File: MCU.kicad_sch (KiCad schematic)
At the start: 44 parts, among them J12 PinHeader_01x03_Pin, SW11 KMR2, SW12 KMR2, U11 W25Q128JVS, U12 RP2350_60QFN, Y11 ABM8_262_T3

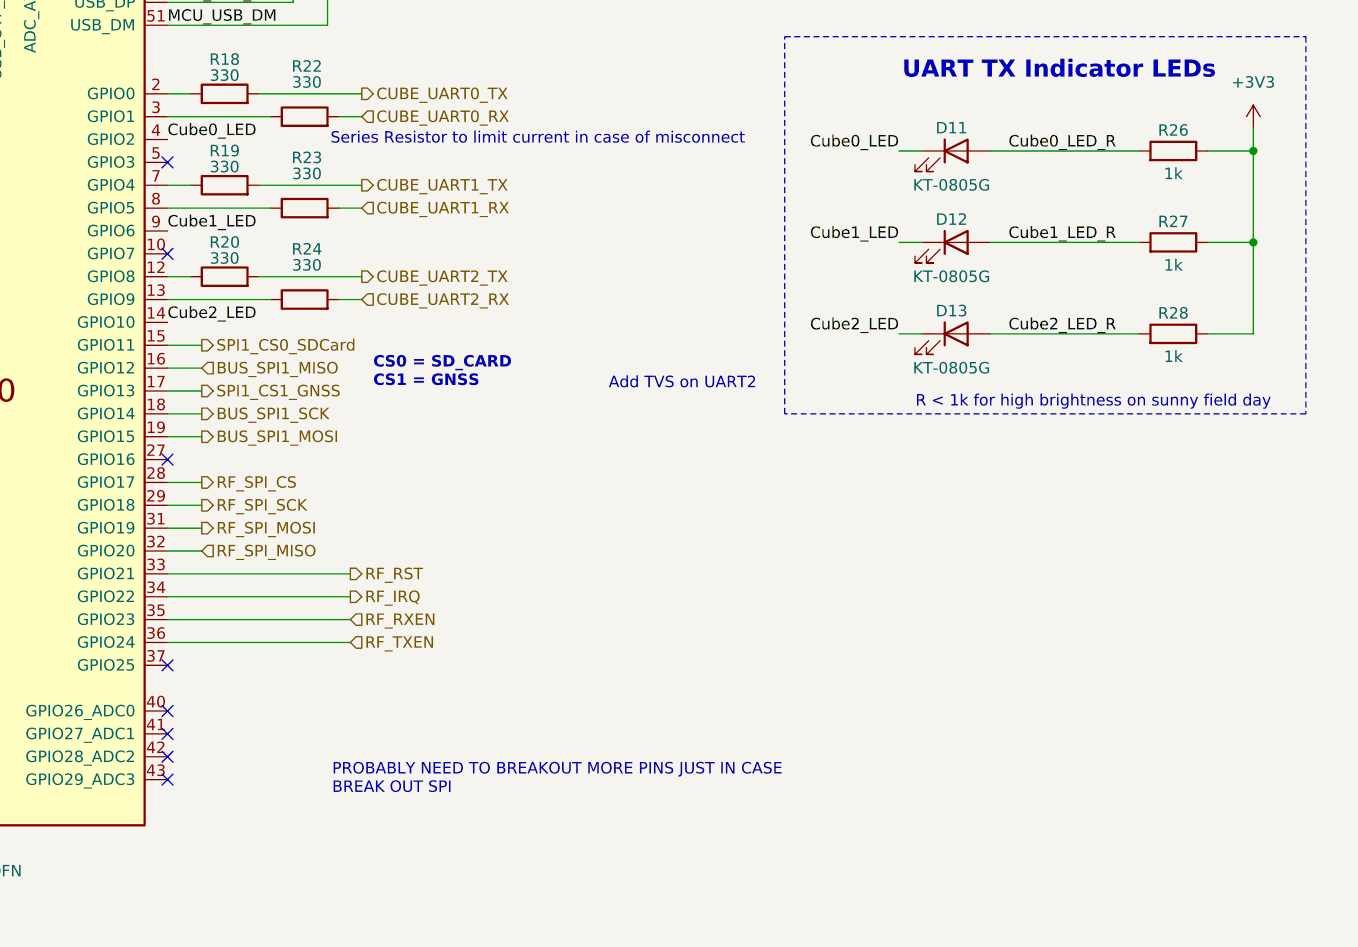
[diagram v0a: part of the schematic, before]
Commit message: discrete protection, charger, ideal diodes, and 5v smps
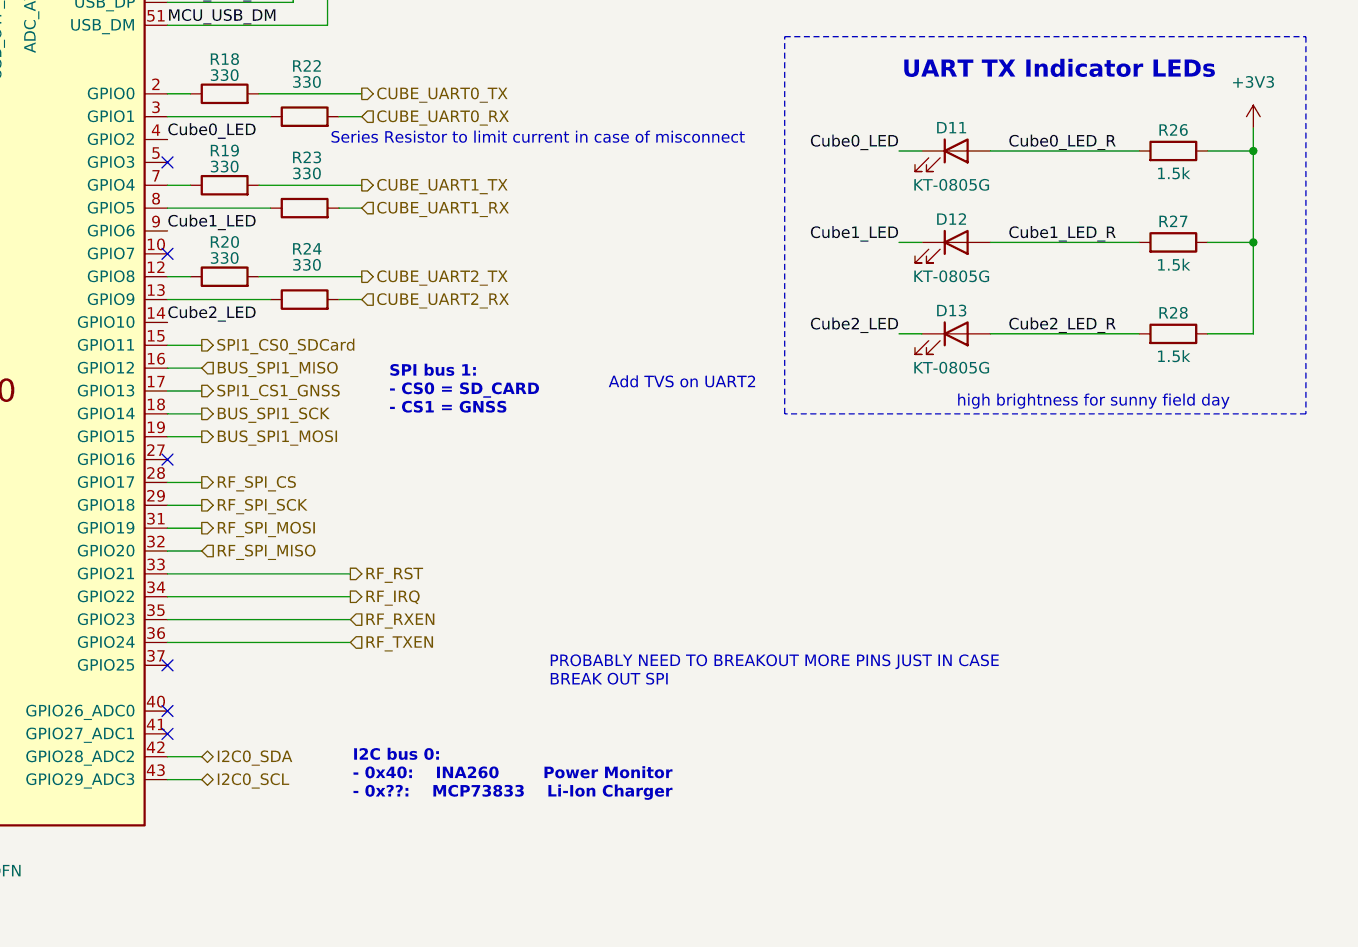
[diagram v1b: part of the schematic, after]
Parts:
- R26, R27, R28: value 1k -> 1.5k
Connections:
- net I2C0_SDA: now reaches U12.42 (GPIO28_ADC2)
- net I2C0_SCL: now reaches U12.43 (GPIO29_ADC3)
- no-connect marks 9 -> 7
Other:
- note added: "I2C bus 0: - 0x40: INA260 Power Monitor - 0x??: MCP73833 Li-Ion Charger"
- note added: "SPI bus 1: - CS0 = SD_CARD - CS1 = GNSS"
- note added: "high brightness for sunny field day"
- note removed: "CS0 = SD_CARD CS1 = GNSS"
- note removed: "R < 1k for high brightness on sunny field day"
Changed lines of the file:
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@@
 	(text "PROBABLY NEED TO BREAKOUT MORE PINS JUST IN CASE\nBREAK OUT SPI"
 		(exclude_from_sim no)
-		(at 262.128 193.04 0)
+		(at 286.258 181.102 0)
 		(effects
 			(font
@@
 		)
 	)
-	(text "CS0 = SD_CARD\nCS1 = GNSS"
+	(text "SPI bus 1:\n- CS0 = SD_CARD\n- CS1 = GNSS"
 		(exclude_from_sim no)
-		(at 266.7 147.828 0)
+		(at 268.478 149.86 0)
 		(effects
 			(font
@@
 		)
 	)
+	(text "I2C bus 0:\n- 0x40:	INA260		Power Monitor\n- 0x??:	MCP73833	Li-Ion Charger"
+		(exclude_from_sim no)
+		(at 264.414 192.532 0)
+		(effects
+			(font
+				(size 1.27 1.27)
+				(thickness 0.254)
+				(bold yes)
+			)
+			(justify left)
+		)
+	)
 	(text "Make sure these R are close to RP2350\n"
 		(exclude_from_sim no)
@@
 		)
 	)
-	(text "R < 1k for high brightness on sunny field day"
+	(text "high brightness for sunny field day"
 		(exclude_from_sim no)
 		(at 346.71 151.13 0)
@@
 	)
 	(no_connect
-		(at 243.84 190.5)
-	)
-	(no_connect
 		(at 243.84 187.96)
 	)
@@
 	)
 	(no_connect
-		(at 243.84 193.04)
-	)
-	(no_connect
 		(at 19.05 121.92)
 	)
@@
 	(wire
 		(pts
+			(xy 247.65 193.04) (xy 243.84 193.04)
+		)
+		(stroke
+			(width 0)
+			(type default)
+		)
+	)
+	(wire
+		(pts
 			(xy 262.89 129.54) (xy 265.43 129.54)
 		)
@@
 	(wire
 		(pts
+			(xy 247.65 190.5) (xy 243.84 190.5)
+		)
+		(stroke
+			(width 0)
+			(type default)
+		)
+	)
+	(wire
+		(pts
 			(xy 127 170.18) (xy 129.54 170.18)
 		)
@@
 		)
 	)
+	(hierarchical_label "I2C0_SDA"
+		(shape bidirectional)
+		(at 247.65 190.5 0)
+		(effects
+			(font
+				(size 1.27 1.27)
+			)
+			(justify left)
+		)
+	)
+	(hierarchical_label "I2C0_SCL"
+		(shape bidirectional)
+		(at 247.65 193.04 0)
+		(effects
+			(font
+				(size 1.27 1.27)
+			)
+			(justify left)
+		)
+	)
 	(hierarchical_label "CUBE_UART0_RX"
 		(shape input)
@@
 			)
 		)
-		(property "Value" "1k"
+		(property "Value" "1.5k"
 			(at 355.6 135.89 90)
 			(effects
@@
 			)
 		)
-		(property "Value" "1k"
+		(property "Value" "1.5k"
 			(at 355.6 125.73 90)
 			(effects
@@
 			)
 		)
-		(property "Value" "1k"
+		(property "Value" "1.5k"
 			(at 355.6 146.05 90)
 			(effects

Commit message: rough power layout
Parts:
- added R1, R2: 10k, symbol Device:R
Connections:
- net +3V3: now also R1.1, R2.1
- net I2C0_SCL: now also R2.2
- net I2C0_SDA: now also R1.2

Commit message: 050326 layouts
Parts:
- R1, R2: footprint (none) -> Resistor_SMD:R_0402_1005Metric
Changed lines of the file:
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@@
 			)
 		)
-		(property "Footprint" ""
+		(property "Footprint" "Resistor_SMD:R_0402_1005Metric"
 			(at 263.398 185.42 90)
 			(effects
@@
 			)
 		)
-		(property "Footprint" ""
+		(property "Footprint" "Resistor_SMD:R_0402_1005Metric"
 			(at 262.382 185.42 90)
 			(effects

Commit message: v2 layouts done
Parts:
- renumbered C11 to C31, C12 to C32, C13 to C33, C14 to C34, C15 to C35, C16 to C36, C17 to C37, C18 to C38, C19 to C39, C20 to C40, C21 to C41, C22 to C42, C23 to C43, C24 to C44, C25 to C45, C26 to C46, D11 to D33, D12 to D34, D13 to D35, J12 to J37, L11 to L31, R11 to R31, R12 to R32, R13 to R33, R14 to R34, R15 to R35, R16 to R36, R17 to R37, R18 to R38, R19 to R39, R20 to R40, R21 to R41, R22 to R42, R23 to R43, R24 to R44, R25 to R45, R1 to R46, R2 to R47, R26 to R48, R27 to R49, R28 to R50, SW11 to SW31, SW12 to SW32, U11 to U31, U12 to U32, Y11 to Y31
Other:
- note added: "I2C bus 0: - 0x18: MCP9808 Temp Sensor - 0x40: INA260 Power Monitor"
- note removed: "I2C bus 0: - 0x40: INA260 Power Monitor - 0x??: MCP73833 Li-Ion Charger"
